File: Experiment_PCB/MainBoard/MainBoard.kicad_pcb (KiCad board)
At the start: 2 copper layers, 98.3 x 162.7 mm, 43 parts, among them U1 Teensy4.1

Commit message: Incorporate feedback
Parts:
- removed R10, R11, R12, R13, R14, R15, R16, R17, R18, R19, R2, R20, R21, R22, R23, R24, R25, R26, R27, R28, R29, R3, R30, R31, R32, R33, R34, R35, R36, R4, R5, R6, R7, R8, R9: 10k, Resistor_SMD:R_0402_1005Metric
- added C1: 10u, Capacitor_SMD:C_0603_1608Metric, F.Cu at (93.5, 144.5)
- added C2: 10u, Capacitor_SMD:C_0603_1608Metric, F.Cu at (91.0, 110.0)
- added C3: 10u, Capacitor_SMD:C_0603_1608Metric, F.Cu at (100.2, 33.5)
- R1: value 10k -> 10
- moved R1 51.9 mm to (140.0, 147.8), turned to 0 degrees
- moved master_connector_input5 0.15 mm to (90.0, 158.5)
- moved master_connector_input6 0.15 mm to (90.0, 158.5)
- moved master_connector_input2 0.07 mm to (90.0, 122.0)
- moved master_connector_input3 0.07 mm to (90.0, 122.0)
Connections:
- R1 pad 1: /CS7 -> VDD
- R1 pad 2: VDD -> 3.3V
- U1 pad 15: VDD -> unconnected-(U1-3V3-Pad15)
- U1 pad 46: VDDIO -> 3.3V
- master_connector_input1 pad 1: VDDIO -> VDD
- master_connector_input1 pad 10: /CS1 -> /CS2
- master_connector_input1 pad 11: /CS2 -> /CS3
- master_connector_input1 pad 12: /CS3 -> /CS4
- master_connector_input1 pad 13: /CS4 -> /CS5
- master_connector_input1 pad 14: /CS5 -> /CS6
- master_connector_input1 pad 3: VDD -> SCK
- master_connector_input1 pad 4: SCK -> MISO
- master_connector_input1 pad 5: MISO -> MOSI
- master_connector_input1 pad 6: MOSI -> SCK1
- master_connector_input1 pad 7: SCK1 -> MISO1
- master_connector_input1 pad 8: MISO1 -> MOSI1
- master_connector_input1 pad 9: MOSI1 -> /CS1
- master_connector_input2 pad 1: VDDIO -> VDD
- master_connector_input2 pad 10: /CS7 -> /CS8
- master_connector_input2 pad 11: /CS8 -> /CS9
- master_connector_input2 pad 12: /CS9 -> /CS10
- master_connector_input2 pad 13: /CS10 -> /CS11
- master_connector_input2 pad 14: /CS11 -> /CS12
- master_connector_input2 pad 3: VDD -> SCK
- master_connector_input2 pad 4: SCK -> MISO
- master_connector_input2 pad 5: MISO -> MOSI
- master_connector_input2 pad 6: MOSI -> SCK1
- master_connector_input2 pad 7: SCK1 -> MISO1
- master_connector_input2 pad 8: MISO1 -> MOSI1
- master_connector_input2 pad 9: MOSI1 -> /CS7
- master_connector_input3 pad 1: VDDIO -> VDD
- master_connector_input3 pad 10: /CS13 -> /CS14
- master_connector_input3 pad 11: /CS14 -> /CS15
- master_connector_input3 pad 12: /CS15 -> /CS16
- master_connector_input3 pad 13: /CS16 -> /CS17
- master_connector_input3 pad 14: /CS17 -> /CS18
- master_connector_input3 pad 3: VDD -> SCK
- master_connector_input3 pad 4: SCK -> MISO
- master_connector_input3 pad 5: MISO -> MOSI
- master_connector_input3 pad 6: MOSI -> SCK1
- master_connector_input3 pad 7: SCK1 -> MISO1
- master_connector_input3 pad 8: MISO1 -> MOSI1
- master_connector_input3 pad 9: MOSI1 -> /CS13
- master_connector_input4 pad 1: VDDIO -> VDD
- master_connector_input4 pad 10: /CS31 -> /CS32
- master_connector_input4 pad 11: /CS32 -> /CS33
- master_connector_input4 pad 12: /CS33 -> /CS34
- master_connector_input4 pad 13: /CS34 -> /CS35
- master_connector_input4 pad 14: /CS35 -> /CS36
- master_connector_input4 pad 3: VDD -> SCK
- master_connector_input4 pad 4: SCK -> MISO
- master_connector_input4 pad 5: MISO -> MOSI
- master_connector_input4 pad 6: MOSI -> SCK1
- master_connector_input4 pad 7: SCK1 -> MISO1
- master_connector_input4 pad 8: MISO1 -> MOSI1
- master_connector_input4 pad 9: MOSI1 -> /CS31
- master_connector_input5 pad 1: VDDIO -> VDD
- master_connector_input5 pad 10: /CS25 -> /CS26
- master_connector_input5 pad 11: /CS26 -> /CS27
- master_connector_input5 pad 12: /CS27 -> /CS28
- master_connector_input5 pad 13: /CS28 -> /CS29
- master_connector_input5 pad 14: /CS29 -> /CS30
- master_connector_input5 pad 3: VDD -> SCK
- master_connector_input5 pad 4: SCK -> MISO
- master_connector_input5 pad 5: MISO -> MOSI
- master_connector_input5 pad 6: MOSI -> SCK1
- master_connector_input5 pad 7: SCK1 -> MISO1
- master_connector_input5 pad 8: MISO1 -> MOSI1
- master_connector_input5 pad 9: MOSI1 -> /CS25
- master_connector_input6 pad 1: VDDIO -> VDD
- master_connector_input6 pad 10: /CS19 -> /CS20
- master_connector_input6 pad 11: /CS20 -> /CS21
- master_connector_input6 pad 12: /CS21 -> /CS22
- master_connector_input6 pad 13: /CS22 -> /CS23
- master_connector_input6 pad 14: /CS23 -> /CS24
- master_connector_input6 pad 3: VDD -> SCK
- master_connector_input6 pad 4: SCK -> MISO
- master_connector_input6 pad 5: MISO -> MOSI
- master_connector_input6 pad 6: MOSI -> SCK1
- master_connector_input6 pad 7: SCK1 -> MISO1
- master_connector_input6 pad 8: MISO1 -> MOSI1
- master_connector_input6 pad 9: MOSI1 -> /CS19
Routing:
- net VDDIO: track 227.9 -> 0.00 mm, vias 9 -> 0
- net VDD: track 363.9 -> 223.6 mm, vias 11 -> 8
- net /CS30: track 172.2 -> 152.5 mm, vias 3 -> 1
- net /CS13: track 87.9 -> 68.4 mm, vias 2 -> 0
- net /CS12: track 85.9 -> 66.5 mm, vias 3 -> 1
- net /CS29: track 158.7 -> 140.1 mm, vias 2 -> 0
- net /CS11: track 85.1 -> 67.0 mm, vias 3 -> 1
- net /CS14: track 85.8 -> 67.8 mm, vias 2 -> 0
- net /CS28: track 152.7 -> 135.5 mm, vias 2 -> 0
- net /CS10: track 84.2 -> 67.4 mm, vias 3 -> 1
- net /CS9: track 86.7 -> 69.9 mm, vias 3 -> 1
- net /CS15: track 84.1 -> 68.0 mm, vias 2 -> 0
- net /CS8: track 86.4 -> 70.4 mm, vias 3 -> 1
- net /CS27: track 146.9 -> 130.9 mm, vias 2 -> 0
- net /CS7: track 86.3 -> 70.8 mm
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- added copper zone on F.Cu, net GND

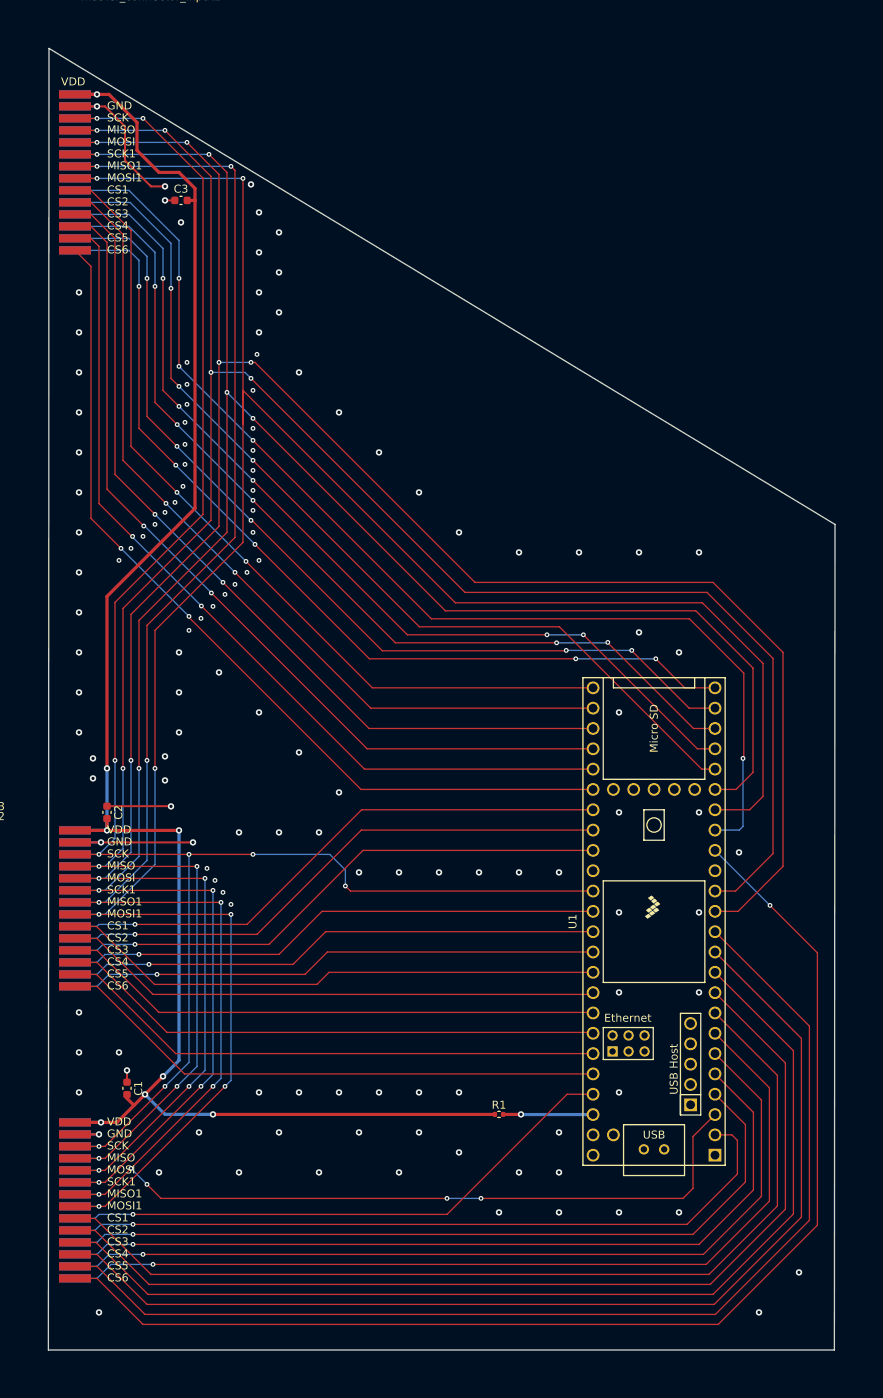
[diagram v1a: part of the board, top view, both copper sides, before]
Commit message: update for file transfer / cleanup some traces
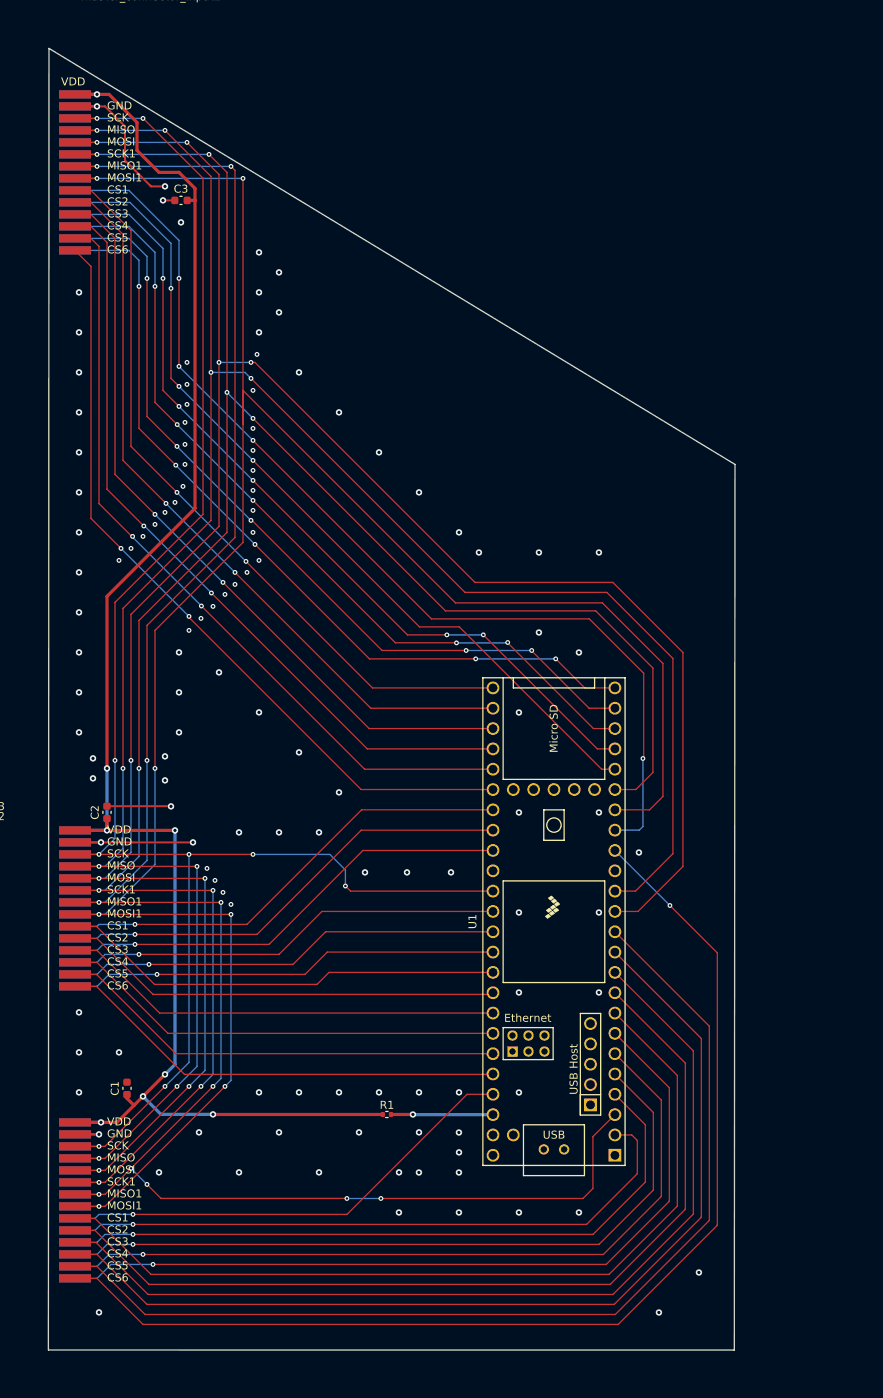
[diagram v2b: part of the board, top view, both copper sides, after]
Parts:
- C1, C2, C3: value 10u -> 1u
- moved R1 14.0 mm to (126.0, 147.8)
- moved U1 12.5 mm to (146.9, 123.7)
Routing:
- net VDD: track 223.6 -> 209.1 mm
- net /CS35: track 116.1 -> 103.6 mm
- net /CS20: track 93.0 -> 80.5 mm
- net /CS30: track 152.5 -> 140.0 mm
- net /CS28: track 135.5 -> 123.0 mm
- net /CS26: track 126.2 -> 113.7 mm
- net /CS24: track 114.6 -> 102.1 mm
- net /CS22: track 104.6 -> 92.1 mm
- net /CS8: track 70.4 -> 57.9 mm
- net /CS19: track 71.2 -> 58.7 mm
- net /CS7: track 70.8 -> 58.3 mm
- net /CS11: track 67.0 -> 54.5 mm
- net /CS9: track 69.9 -> 57.4 mm
- net /CS13: track 68.4 -> 55.9 mm
- net /CS12: track 66.5 -> 54.0 mm
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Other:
- board size 98.3 x 162.7 mm -> 85.8 x 162.7 mm

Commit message: transfer files to laptop for order
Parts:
- added REF**: MountingHole_2.2mm_M2_ISO7380, MountingHole:MountingHole_2.2mm_M2_ISO7380, F.Cu at (162.8, 70.8)
- added REF**: MountingHole_2.2mm_M2_ISO7380, MountingHole:MountingHole_2.2mm_M2_ISO7380, F.Cu at (80.2, 90.2)
- added REF**: MountingHole_2.2mm_M2_ISO7380, MountingHole:MountingHole_2.2mm_M2_ISO7380, F.Cu at (98.5, 182.2)
- added REF**: MountingHole_2.2mm_M2_ISO7380, MountingHole:MountingHole_2.2mm_M2_ISO7380, F.Cu at (164.5, 172.2)
- moved C3 8.26 mm to (96.2, 26.3), turned to 90 degrees
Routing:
- net MISO: track 287.0 -> 308.4 mm, vias 9 -> 8
- net MOSI: track 295.3 -> 313.9 mm, vias 9 -> 8
- net SCK1: track 274.8 -> 289.9 mm, vias 9 -> 8
- net MISO1: track 262.6 -> 248.8 mm, vias 11 -> 10
- net VDD: track 209.1 -> 220.5 mm
- net MOSI1: track 290.1 -> 297.0 mm, vias 7 -> 8
- net GND: track 54.1 -> 60.2 mm, vias 122 -> 79
- net SCK: track 217.7 -> 214.9 mm, vias 9 -> 8
- net /CS1: track 93.8 -> 94.5 mm, vias 2 -> 0
- net /CS36: track 102.4 -> 103.0 mm, vias 5 -> 3
- net /CS34: track 104.5 -> 105.1 mm, vias 5 -> 3
- net /CS31: track 128.2 -> 128.7 mm, vias 4 -> 2
- net /CS2: track 95.0 -> 95.5 mm, vias 2 -> 0
- net /CS4: track 97.4 -> 97.8 mm, vias 2 -> 0
- net /CS5: track 98.6 -> 99.0 mm, vias 2 -> 0
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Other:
- board size 85.8 x 162.7 mm -> 95.8 x 162.7 mm

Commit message: Ordered PCBs
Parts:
- added REF**: MountingHole_2.2mm_M2_ISO7380, MountingHole:MountingHole_2.2mm_M2_ISO7380, F.Cu at (135.0, 53.0)
- added REF**: MountingHole_2.2mm_M2_ISO7380, MountingHole:MountingHole_2.2mm_M2_ISO7380, F.Cu at (112.6, 152.8)
- added REF**: MountingHole_2.2mm_M2_ISO7380, MountingHole:MountingHole_2.2mm_M2_ISO7380, F.Cu at (108.5, 37.0)
- moved REF** 12.0 mm to (91.2, 172.8)
- moved REF** 0.35 mm to (80.0, 90.0)
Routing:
- net GND: track 60.2 -> 60.7 mm, vias 79 -> 78
